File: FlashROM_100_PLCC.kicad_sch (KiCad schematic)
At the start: 6 parts

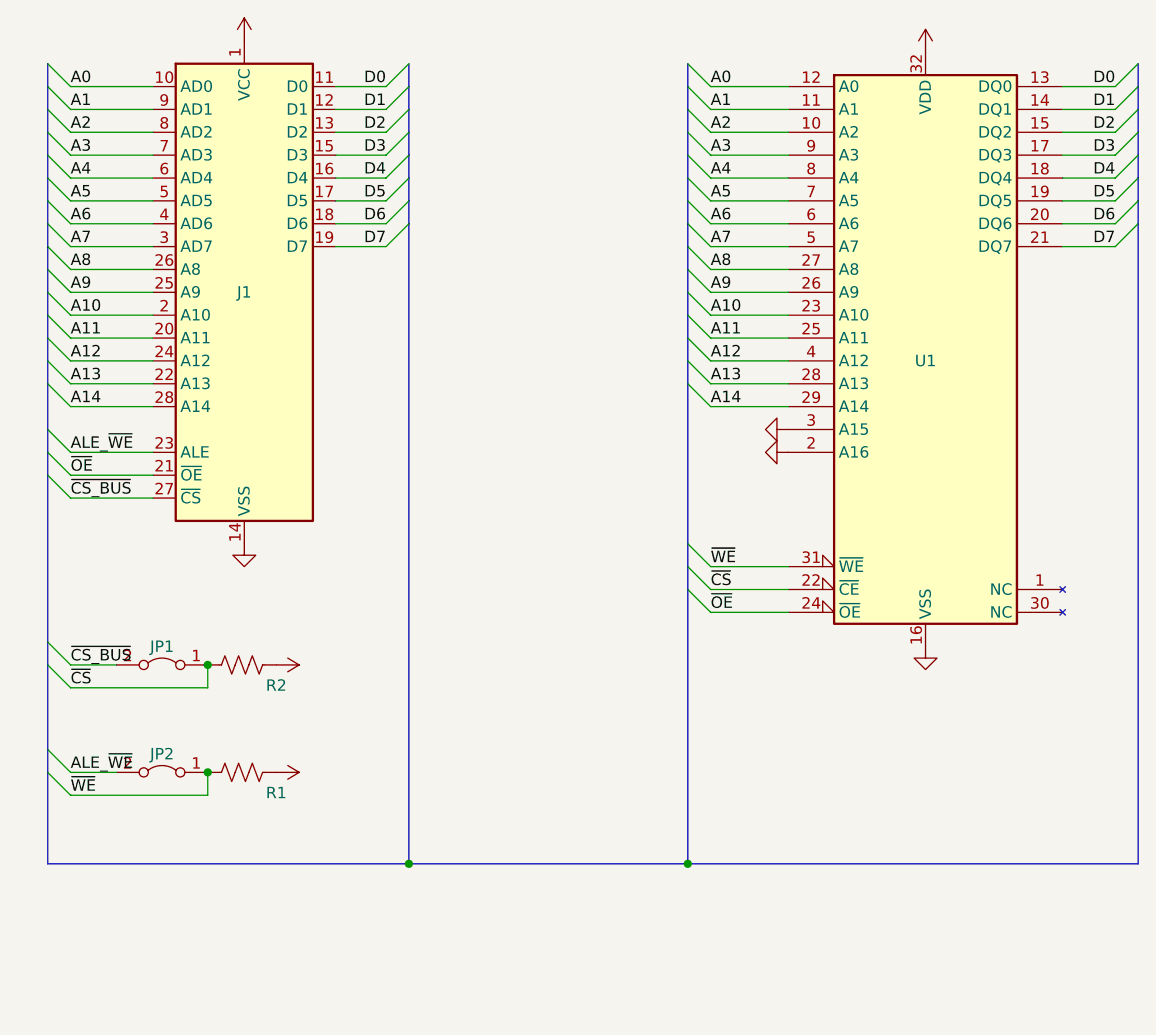
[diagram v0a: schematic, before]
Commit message: flashrom_100_plcc outline
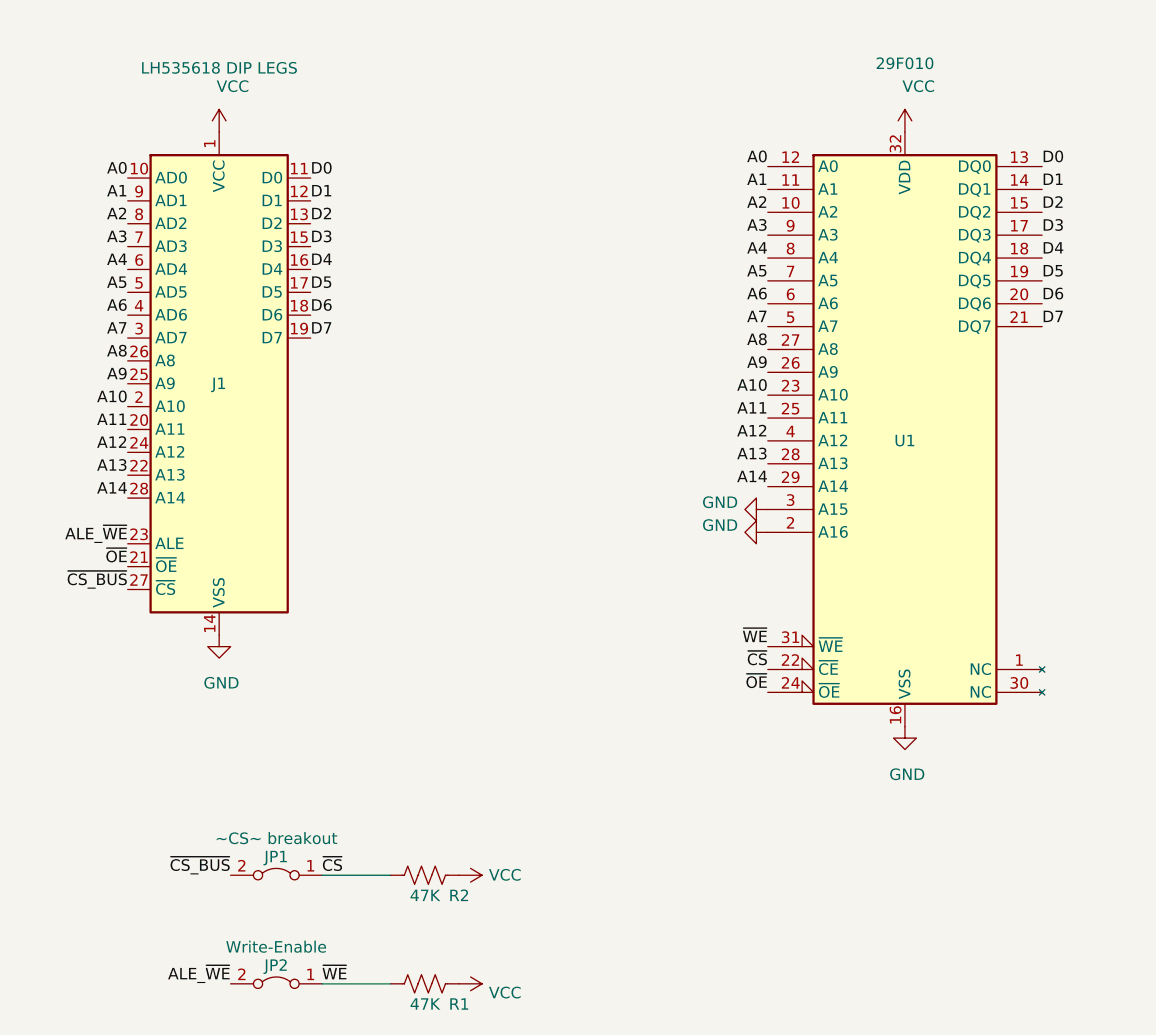
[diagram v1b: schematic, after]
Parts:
- J1: value (none) -> LH535618 DIP LEGS; footprint (none) -> 000_LOCAL:DIP28_0.6_pcb
- JP1: value (none) -> ~CS~ breakout; footprint (none) -> 000_LOCAL:Pin_Header_Angled_1x02_Pitch2.54mm
- JP2: value (none) -> Write-Enable; footprint (none) -> 000_LOCAL:Pin_Header_Angled_1x02_Pitch2.54mm
- R1, R2: value (none) -> 47K; footprint (none) -> 000_LOCAL:R_0805
- U1: value (none) -> 29F010; footprint (none) -> 000_LOCAL:PLCC32_7x9
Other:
- moved on the sheet: J1, JP1, JP2, R1, R2, U1

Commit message: various minor cleanups
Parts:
- JP1: value ~CS~ breakout -> ~{CS} breakout
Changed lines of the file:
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@@
     (in_bom yes) (on_board yes)
     (property "Reference" "JP1" (id 0) (at 101.6 144.018 0))
-    (property "Value" "~CS~ breakout" (id 1) (at 101.6 141.986 0))
+    (property "Value" "~{CS} breakout" (id 1) (at 101.6 141.986 0))
     (property "Footprint" "000_LOCAL:Pin_Header_Angled_1x02_Pitch2.54mm" (id 2) (at 101.6 146.05 0)
       (effects (font (size 1.27 1.27)) hide)
@@
     )
     (path "/00000000-0000-0000-0000-00005e68b8a2"
-      (reference "JP1") (unit 1) (value "~CS~ breakout") (footprint "000_LOCAL:Pin_Header_Angled_1x02_Pitch2.54mm")
+      (reference "JP1") (unit 1) (value "~{CS} breakout") (footprint "000_LOCAL:Pin_Header_Angled_1x02_Pitch2.54mm")
     )
     (path "/00000000-0000-0000-0000-00005fbc3795"

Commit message: flashrom_100 pin names & minor trace move
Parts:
- R1, R2: value 47K -> 100K
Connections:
- net ~{CS} renamed ~{CS_IC}
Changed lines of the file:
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@@
     (effects (font (size 1.27 1.27)) (justify left bottom))
   )
-  (label "~{CS}" (at 106.68 146.05 0)
+  (label "~{CS_IC}" (at 106.68 146.05 0)
     (effects (font (size 1.27 1.27)) (justify left bottom))
   )
@@
     (effects (font (size 1.27 1.27)) (justify right bottom))
   )
-  (label "~{CS}" (at 156.21 123.19 180)
+  (label "~{CS_IC}" (at 156.21 123.19 180)
     (effects (font (size 1.27 1.27)) (justify right bottom))
   )
@@
     (in_bom yes) (on_board yes)
     (property "Reference" "R2" (id 0) (at 121.92 148.336 90))
-    (property "Value" "47K" (id 1) (at 118.11 148.336 90))
+    (property "Value" "100K" (id 1) (at 118.11 148.336 90))
     (property "Footprint" "000_LOCAL:R_0805" (id 2) (at 118.11 146.05 0)
       (effects (font (size 1.27 1.27)) hide)
@@
     (in_bom yes) (on_board yes)
     (property "Reference" "R1" (id 0) (at 121.92 160.401 90))
-    (property "Value" "47K" (id 1) (at 118.11 160.401 90))
+    (property "Value" "100K" (id 1) (at 118.11 160.401 90))
     (property "Footprint" "000_LOCAL:R_0805" (id 2) (at 118.11 158.115 0)
       (effects (font (size 1.27 1.27)) hide)
@@
     )
     (path "/00000000-0000-0000-0000-00005e6b3af8"
-      (reference "R1") (unit 1) (value "47K") (footprint "000_LOCAL:R_0805")
+      (reference "R1") (unit 1) (value "100K") (footprint "000_LOCAL:R_0805")
     )
     (path "/00000000-0000-0000-0000-00005e68c7f8"
-      (reference "R2") (unit 1) (value "47K") (footprint "000_LOCAL:R_0805")
+      (reference "R2") (unit 1) (value "100K") (footprint "000_LOCAL:R_0805")
     )
     (path "/00000000-0000-0000-0000-00005e5b130a"
